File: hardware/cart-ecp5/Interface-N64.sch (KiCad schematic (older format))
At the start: 10 parts, among them J3 N64_Cartridge_Bus, U4 ATtiny25-20SU

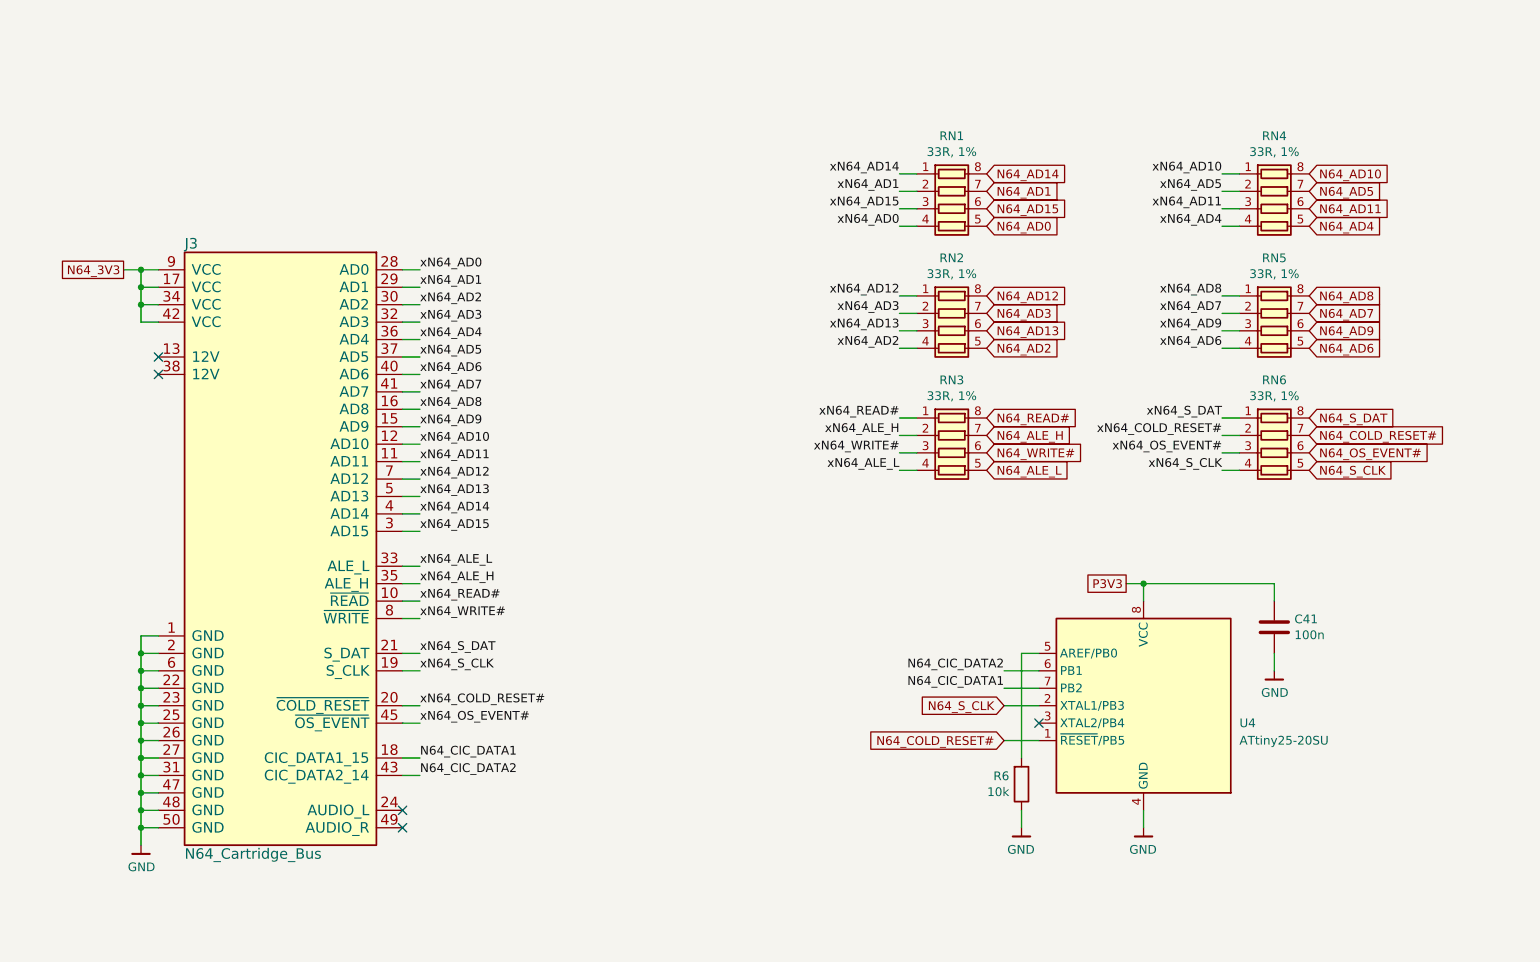
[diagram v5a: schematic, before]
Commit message: Assign FPGA IO for N64_CIC_DATA[12] and add series termination
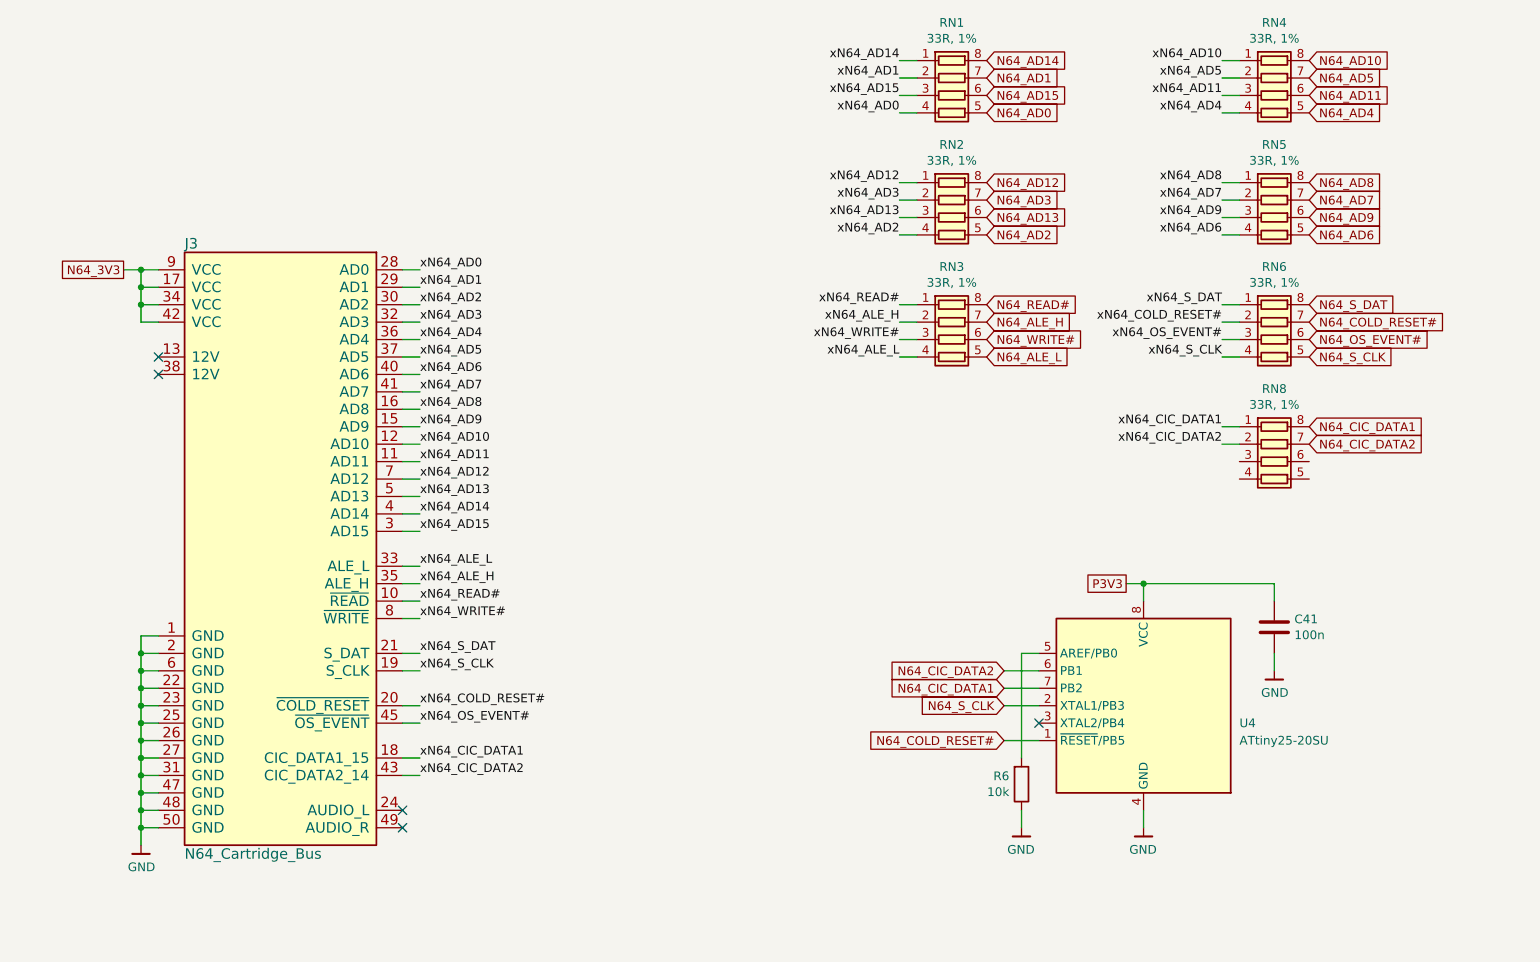
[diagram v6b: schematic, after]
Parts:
- added RN8: 33R, 1%, Resistor_SMD:R_Array_Convex_4x0603, symbol Device:R_Pack04
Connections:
- net N64_CIC_DATA1: now also RN8.8 (R1.2); no longer J3.18 (CIC_DATA1_15)
- net N64_CIC_DATA2: now also RN8.7 (R2.2); no longer J3.43 (CIC_DATA2_14)
- new net xN64_CIC_DATA1: J3.18 (CIC_DATA1_15), RN8.1 (R1.1)
- new net xN64_CIC_DATA2: J3.43 (CIC_DATA2_14), RN8.2 (R2.1)
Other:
- moved on the sheet: RN1, RN2, RN3, RN4, RN5, RN6

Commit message: Check all resistor values for power management and assign MPN for caps and resistors
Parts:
- C41: MFR (none) -> Samsung; MPN (none) -> CL05B104KO5NNNC
- R6: MFR (none) -> Yageo; MPN (none) -> RC0402FR-0710KL
- RN4, RN5, RN6, RN7, RN8, RN9: MFR (none) -> Yageo
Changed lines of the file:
@@
 F 3 "~" H 7000 1450 50  0001 C CNN
 F 4 "YC164-FR-0733RL" H 7000 1450 50  0001 C CNN "MPN"
+F 5 "Yageo" H 7000 1450 50  0001 C CNN "MFR"
 	1    7000 1450
 	0    1    1    0
@@
 F 3 "~" H 7000 2150 50  0001 C CNN
 F 4 "YC164-FR-0733RL" H 7000 2150 50  0001 C CNN "MPN"
+F 5 "Yageo" H 7000 2150 50  0001 C CNN "MFR"
 	1    7000 2150
 	0    1    1    0
@@
 F 3 "~" H 7000 2850 50  0001 C CNN
 F 4 "YC164-FR-0733RL" H 7000 2850 50  0001 C CNN "MPN"
+F 5 "Yageo" H 7000 2850 50  0001 C CNN "MFR"
 	1    7000 2850
 	0    1    1    0
@@
 F 3 "~" H 8850 1450 50  0001 C CNN
 F 4 "YC164-FR-0733RL" H 8850 1450 50  0001 C CNN "MPN"
+F 5 "Yageo" H 8850 1450 50  0001 C CNN "MFR"
 	1    8850 1450
 	0    1    1    0
@@
 F 3 "~" H 8850 2150 50  0001 C CNN
 F 4 "YC164-FR-0733RL" H 8850 2150 50  0001 C CNN "MPN"
+F 5 "Yageo" H 8850 2150 50  0001 C CNN "MFR"
 	1    8850 2150
 	0    1    1    0
@@
 F 3 "~" H 8850 2850 50  0001 C CNN
 F 4 "YC164-FR-0733RL" H 8850 2850 50  0001 C CNN "MPN"
+F 5 "Yageo" H 8850 2850 50  0001 C CNN "MFR"
 	1    8850 2850
 	0    1    1    0
@@
 F 2 "Resistor_SMD:R_0402_1005Metric" V 7330 5400 50  0001 C CNN
 F 3 "~" H 7400 5400 50  0001 C CNN
+F 4 "RC0402FR-0710KL" H 7400 5400 50  0001 C CNN "MPN"
+F 5 "Yageo" H 7400 5400 50  0001 C CNN "MFR"
 	1    7400 5400
 	1    0    0    1
@@
 F 2 "Capacitor_SMD:C_0402_1005Metric" H 8888 4350 50  0001 C CNN
 F 3 "~" H 8850 4500 50  0001 C CNN
+F 4 "Samsung" H 8850 4500 50  0001 C CNN "MFR"
+F 5 "CL05B104KO5NNNC" H 8850 4500 50  0001 C CNN "MPN"
 	1    8850 4500
 	1    0    0    -1
@@
 F 3 "~" H 8850 3550 50  0001 C CNN
 F 4 "YC164-FR-0733RL" H 8850 3550 50  0001 C CNN "MPN"
+F 5 "Yageo" H 8850 3550 50  0001 C CNN "MFR"
 	1    8850 3550
 	0    1    1    0
